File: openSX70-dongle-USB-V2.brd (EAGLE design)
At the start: 20 x 45 mm, 29 parts, among them J1 687106183722, J2 SJ-3523-SMT-TR, U1 FT232RLSSOP

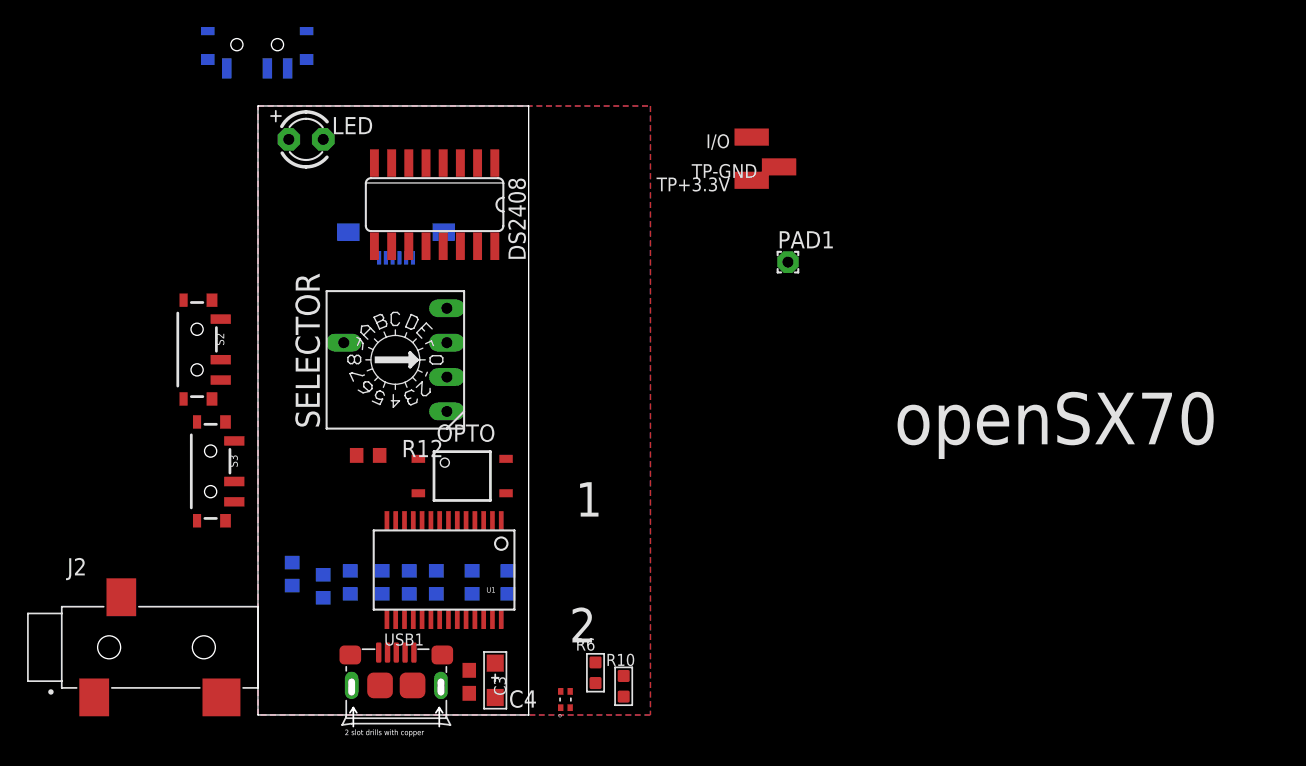
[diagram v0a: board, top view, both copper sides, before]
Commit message: new design, new parts
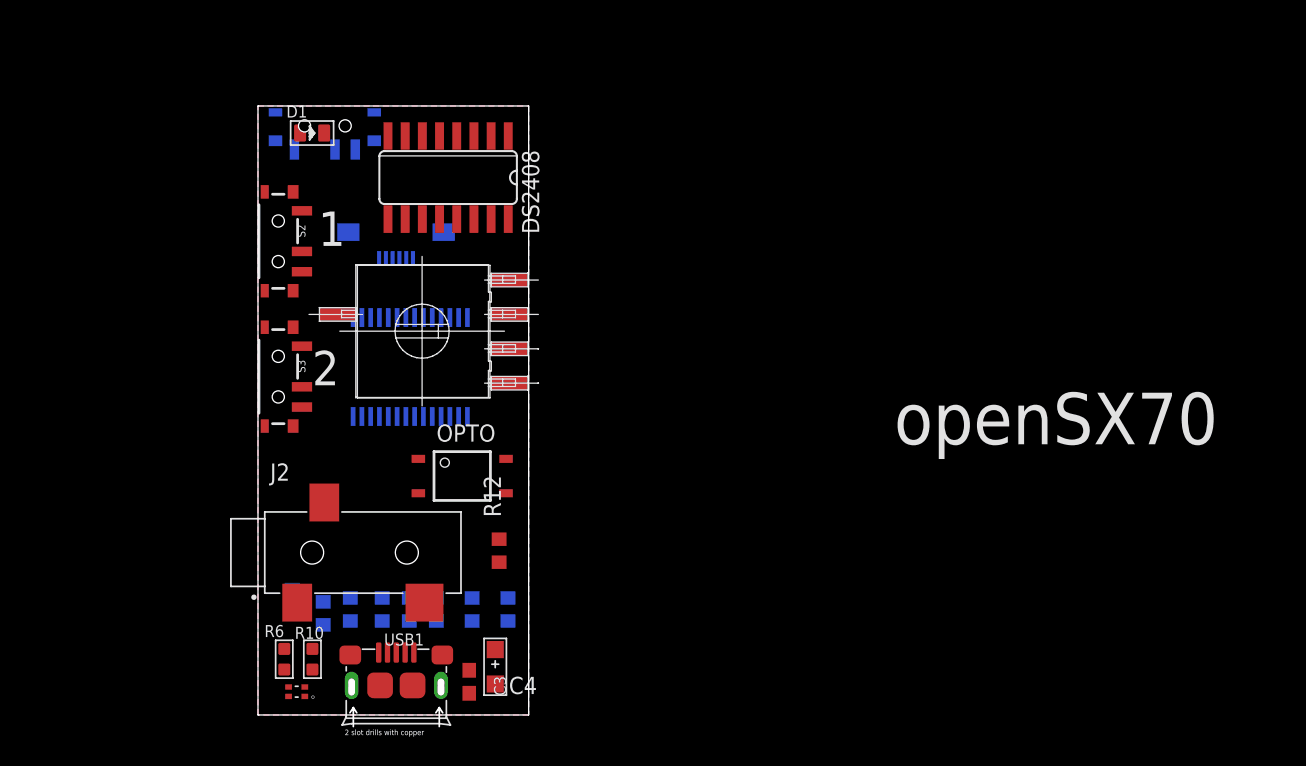
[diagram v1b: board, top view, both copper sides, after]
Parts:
- removed I/O, TP+3.3V, TP-GND: (no value), wirepad:SMD1,27-2,54
- removed LED: (no value), adafruit:LED3MM
- removed PAD1: WIREPAD1,6/0,8, wirepad:1,6/0,8
- added D1: YELLOW-0805, Seeed-LED-2016:LED-0805
- SELECTOR: value (none) -> A6RS; device special:SW-C16 -> _openSX70:A6RS-161RS
- moved R10 23.1 mm to (4.02, 4.12)
- moved R6 23.0 mm to (1.94, 4.12)
- moved U$1 19.9 mm to (2.86, 1.72), turned to 180 degrees
- moved J2 16.6 mm to (4.00, 12.0)
- moved U1 15.2 mm to (11.2, 25.7), flipped to the bottom
- moved R12 12.0 mm to (17.8, 12.1), turned to 90 degrees
- moved S2 10.0 mm to (1.50, 35.0)
- moved S3 8.60 mm to (1.50, 25.0)
- moved S1 7.81 mm to (4.94, 43.5)
- moved SELECTOR 7.62 mm to (17.1, 23.2)
- moved DS2408 2.24 mm to (14.1, 39.7)
- moved R1 2.00 mm to (2.53, 8.41)
- moved R9 2.00 mm to (4.82, 7.51)
- moved R2 2.00 mm to (15.8, 7.80)
- moved R3 2.00 mm to (11.2, 7.80)
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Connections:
- net 1W: no longer I/O.1
- net 3V3OUT: now also D1.+; no longer LED.A, PAD1.1, TP+3.3V.1
- net GND: no longer TP-GND.1
- net N$2: now also D1.-; no longer LED.K

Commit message: 20x45pcb
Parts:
- moved R12 10.1 mm to (9.14, 17.4), turned to 0 degrees
- moved D1 2.00 mm to (4.00, 41.0)
- moved OPTO 2.00 mm to (15.1, 20.3)
- moved U1 2.00 mm to (11.2, 23.7)
- moved R4 0.75 mm to (13.9, 7.96)
- moved C4 0.54 mm to (17.8, 3.11)
- moved R3 0.49 mm to (11.6, 7.96)
- moved DS2408 0.45 mm to (13.6, 39.7), turned to 0 degrees
- moved R9 0.45 mm to (4.81, 7.96)
- moved R1 0.45 mm to (2.53, 7.96)
- moved R2 0.41 mm to (16.2, 7.96)
- moved J1 0.38 mm to (10.0, 36.0)
- moved R7 0.31 mm to (7.08, 7.96)
- moved R5 0.24 mm to (9.36, 7.96)
- moved R8 0.16 mm to (18.5, 7.96)
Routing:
- net 5V: track 0.00 -> 81.1 mm, vias 0 -> 8
- net 3V3OUT: track 0.00 -> 71.8 mm, vias 0 -> 7
- net N$4: track 0.00 -> 61.6 mm, vias 0 -> 7
- net N$6: track 0.00 -> 57.9 mm, vias 0 -> 6
- net VCC-USB: track 0.00 -> 55.8 mm, vias 0 -> 7
- net N$7: track 0.00 -> 50.4 mm, vias 0 -> 5
- net N$2: track 0.00 -> 44.3 mm, vias 0 -> 5
- net N$3: track 0.00 -> 43.5 mm, vias 0 -> 5
- net N$13: track 0.00 -> 43.1 mm, vias 0 -> 2
- net N$5: track 0.00 -> 42.8 mm, vias 0 -> 5
- net N$8: track 0.00 -> 40.6 mm, vias 0 -> 1
- net 1W: track 0.00 -> 37.5 mm, vias 0 -> 2
- net TXLED: track 0.00 -> 30.8 mm, vias 0 -> 1
- net N$1: track 0.00 -> 30.4 mm
- net N$16: track 0.00 -> 26.2 mm, vias 0 -> 1
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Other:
- board text removed: "openSX70"
